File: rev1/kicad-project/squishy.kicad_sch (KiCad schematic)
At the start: 62 parts, among them J1 USB_B_Micro, J2 Conn_02x26_Top_Bottom, J3 Conn_01x04, J4 Conn_02x05_Odd_Even, Q1 Q_PMOS_DGS, Q5 Q_NMOS_GSD, U12 SP3400-02UTG, U14 USB3318, U19 ICE40HX8K-BG121, U26 W25N01GVZEIG, X1 16MHz, X2 48MHz

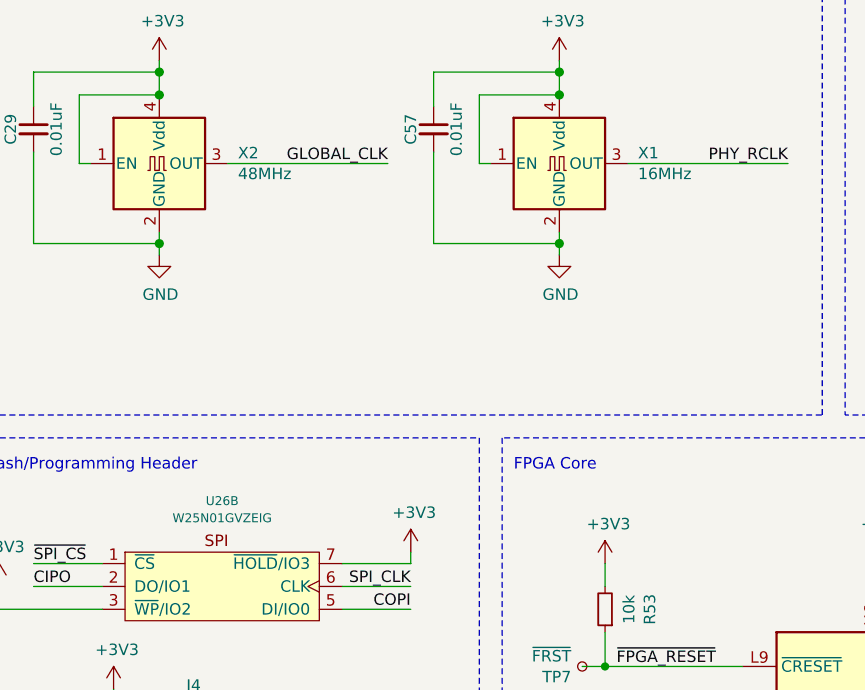
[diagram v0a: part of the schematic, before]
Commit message: hardware: rev1: Updated the SPI flash and ULPI osc, this closes #2
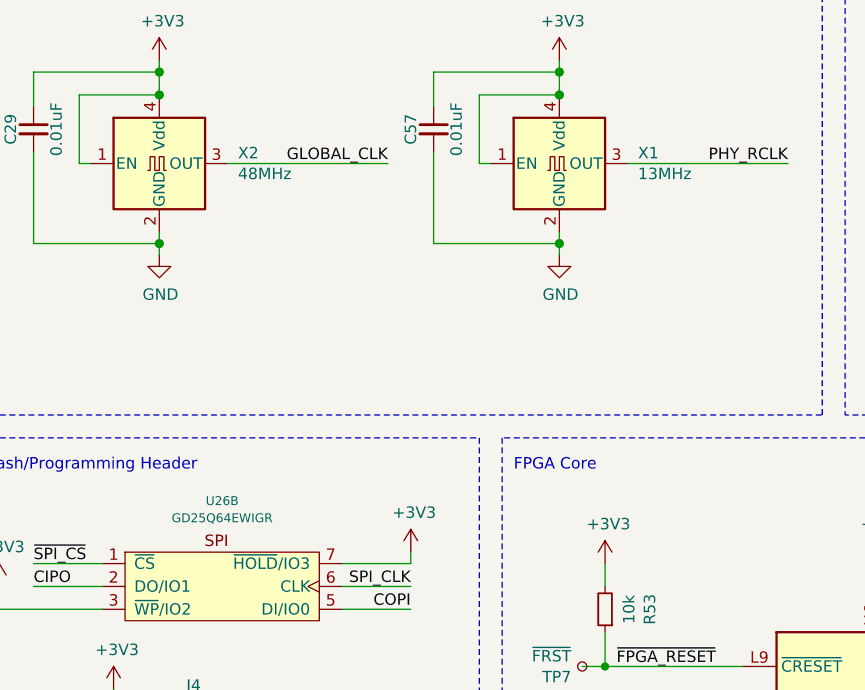
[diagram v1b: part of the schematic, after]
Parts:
- U26: value W25N01GVZEIG -> GD25Q64EWIGR; footprint lethalbit-memory:WSON-8-1EP-6.0x8.0mm -> rhais_package-qfn:UDFN-8-1EP_6x5mm_P1.27mm_EP3.4x4mm; MFR Winbond -> GigaDevice; MPN W25N01GVZEIG TR -> GD25Q64EWIGR
- X1: value 16MHz -> 13MHz; footprint Oscillator:Oscillator_SMD_Abracon_ASE-4Pin_3.2x2.5mm -> rhais_osc:SMD3225; MFR Abracon -> (none); MPN ASEMB-16.000MHZ-LY-T -> (none)
